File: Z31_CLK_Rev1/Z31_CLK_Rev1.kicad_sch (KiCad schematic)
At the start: 16 parts, among them J1 Conn_01x06_Male, J2 ICSP, U1 MAX6922, U2 4BT-78Z_6L, U3 ATMEGA328-AURCT-ND, U4 MCP2510, U5 TJR1443, Y1 8MHz, Y2 16MHz

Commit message: add code
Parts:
- removed C4: 100n, Capacitor_SMD:C_0805_2012Metric_Pad1.18x1.45mm_HandSolder, symbol Device:C_Small
- removed U1: MAX6922, Package_LCC:PLCC-44_16.6x16.6mm_P1.27mm, symbol Personal:MAX6922
- removed U2: 4BT-78Z_6L, Personal:4BT-78Z_6L, symbol Personal:4BT-78Z_6L

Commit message: Catchup
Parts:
- removed C2, C3: 100n, Capacitor_SMD:C_0805_2012Metric_Pad1.18x1.45mm_HandSolder, symbol Device:C_Small
- removed U4: MCP2510, Package_SO:TSSOP-20_4.4x6.5mm_P0.65mm, symbol Personal:MCP2510
- removed U5: TJR1443, Package_SO:SO-14_3.9x8.65mm_P1.27mm, symbol Personal:TJR1443
- removed Y1: 8MHz, Crystal:Crystal_SMD_HC49-SD, symbol Device:Crystal_Small
- added C1, C2: 100nF, Capacitor_SMD:C_0805_2012Metric_Pad1.18x1.45mm_HandSolder, symbol Device:C
- added C10, C8: 100nF, Capacitor_SMD:C_0805_2012Metric_Pad1.18x1.45mm_HandSolder, symbol Device:C_Small
- added C11: 22uF, Capacitor_SMD:CP_Elec_5x5.7, symbol Device:C_Polarized_Small
- added C12: N/A, Capacitor_SMD:C_0805_2012Metric_Pad1.18x1.45mm_HandSolder, symbol Device:C_Small
- added C13: yes, Capacitor_SMD:C_1210_3225Metric_Pad1.33x2.70mm_HandSolder, symbol Device:C_Small
- added C4: 10pF, Capacitor_SMD:C_0805_2012Metric_Pad1.18x1.45mm_HandSolder, symbol Device:C_Small
- added C9: 1u, Capacitor_SMD:C_1210_3225Metric_Pad1.33x2.70mm_HandSolder, symbol Device:C_Small
- added D1: D_Schottky, Diode_SMD:D_SMA, symbol Device:D_Schottky
- added D2: SMAJ18CAQ-13-F, Diode_SMD:D_SMA, symbol Device:D_TVS
- added F1: Polyfuse, Fuse:Fuse_1812_4532Metric_Pad1.30x3.40mm_HandSolder, symbol Device:Polyfuse
- added R1: 47K, Resistor_SMD:R_0805_2012Metric_Pad1.20x1.40mm_HandSolder, symbol Device:R
- added R2, R3: R, Resistor_SMD:R_0805_2012Metric_Pad1.20x1.40mm_HandSolder, symbol Device:R
- added R4: 10k, Resistor_SMD:R_0805_2012Metric_Pad1.20x1.40mm_HandSolder, symbol Device:R_Small
- added R5, R6: N/A, Resistor_SMD:R_0805_2012Metric_Pad1.20x1.40mm_HandSolder, symbol Device:R_Small
- added SW?: Hour, symbol Switch:SW_Push
- added SW?: Select, symbol Switch:SW_Push
- added SW?: Reset, symbol Switch:SW_Push
- added SW?: Minute, symbol Switch:SW_Push
- added TH1: NTC 47K, Resistor_SMD:R_0805_2012Metric_Pad1.20x1.40mm_HandSolder, symbol Device:Thermistor_NTC
- added U2: HCMS-291x, symbol Personal:HCMS-291x
- added U3: MCP2515-xST, Package_SO:TSSOP-20_4.4x6.5mm_P0.65mm, symbol Interface_CAN_LIN:MCP2515-xST
- added U4: TJR1443, Package_SO:SO-14_3.9x8.65mm_P1.27mm, symbol Personal:TJR1443
- added U5: NCV4276B, Package_TO_SOT_SMD:TO-263-5_TabPin3, symbol Personal:NCV4276B
- added Y2: 8MHz, Crystal:Crystal_SMD_HC49-SD, symbol Device:Crystal_Small
- C5: value 100n -> 10pF
- C6, C7: value 20p -> 100nF
- renumbered C1 to C3, J2 to J1, J1 to J2, U3 to U1, Y2 to Y1
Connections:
- net +12V_CONST: now also F1.2
- net +5V: now also C6.2, C7.2, C12.1, C13.1, C8.2, R1.1, R5.1, U2.10 (V_{LED}), U2.22 (V_{Logic}), U2.3 (V_{LED}), U3.20 (VDD), U4.3 (Vcc), U4.5 (Vio), U5.5 (OUT)
- net CANH: now also U4.13 (CANH)
- net CANL: now also U4.12 (CANL)
- net CAN_INT: now also U3.13 (~{INT})
- net CS_CAN: now also U3.18 (~{CS})
- net GND: now also C5.1, C1.2, C10.2, C11.2, C13.2, C2.2, C4.1, C8.1, C9.2, D2.1 (A1), R3.2, R4.2, R6.2, TH1.2, U2.20 (GND_{Logic}), U2.7 (GND_{LED}), U3.10 (VSS), U4.2 (GND), U5.3 (GND); no longer C5.2
- net MISO: now also U3.17 (SO)
- net MOSI: now also U3.16 (SI)
- net SCK: now also U3.14 (SCK)
- net at U1.20 (AREF): no longer C5.1
- net MODULE_TEMPERATURE: now reaches U1.19 (ADC6)
- net MODULE_TEMPERATURE: now also C1.1, R1.2, TH1.1
- net MODULE_VOLTAGE: now reaches U1.22 (ADC7)
- net MODULE_VOLTAGE: now also C2.1, R2.2, R3.1, U4.9 (WAKE)
- net VFBLANK: no longer names the net of U1.9 (PD5)
- new net: R4.1, U4.7 (INH), U5.2 (~{INH})
- new net: C12.2, R5.2, R6.1, U5.4 (VA)
- new net: SW?.1, SW?.1
- new net: SW?.1, SW?.2 (x2)
- new net: SW?.2, SW?.2
- new net: D1.2 (A), D2.2 (A2), F1.1
- new net: C5.2, U3.9 (OSC1), Y2.1
- new net: C4.2, U3.8 (OSC2), Y2.2
- new net +12V: C10.1, C11.1, C9.1, D1.1 (K), U4.10 (Vbat), U5.1 (IN)
- new net +12V_IGN: R2.1
- new net CAN_EN: U3.12 (~{RX0BF}), U4.6 (EN)
- new net CAN_ERR: U3.4 (~{TX0RTS}), U4.8 (~{ERR})
- new net CAN_STB: U3.11 (~{RX1BF}), U4.14 (~{STB_N})
- new net RESET_CAN: U3.19 (~{RESET})
- new net RXCAN: U3.2 (RXCAN), U4.4 (RXCAN)
- new net TXCAN: U3.1 (TXCAN), U4.1 (TXCAN)
- no-connect marks 0 -> 5
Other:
- moved on the sheet: C3, J2, U1, Y1

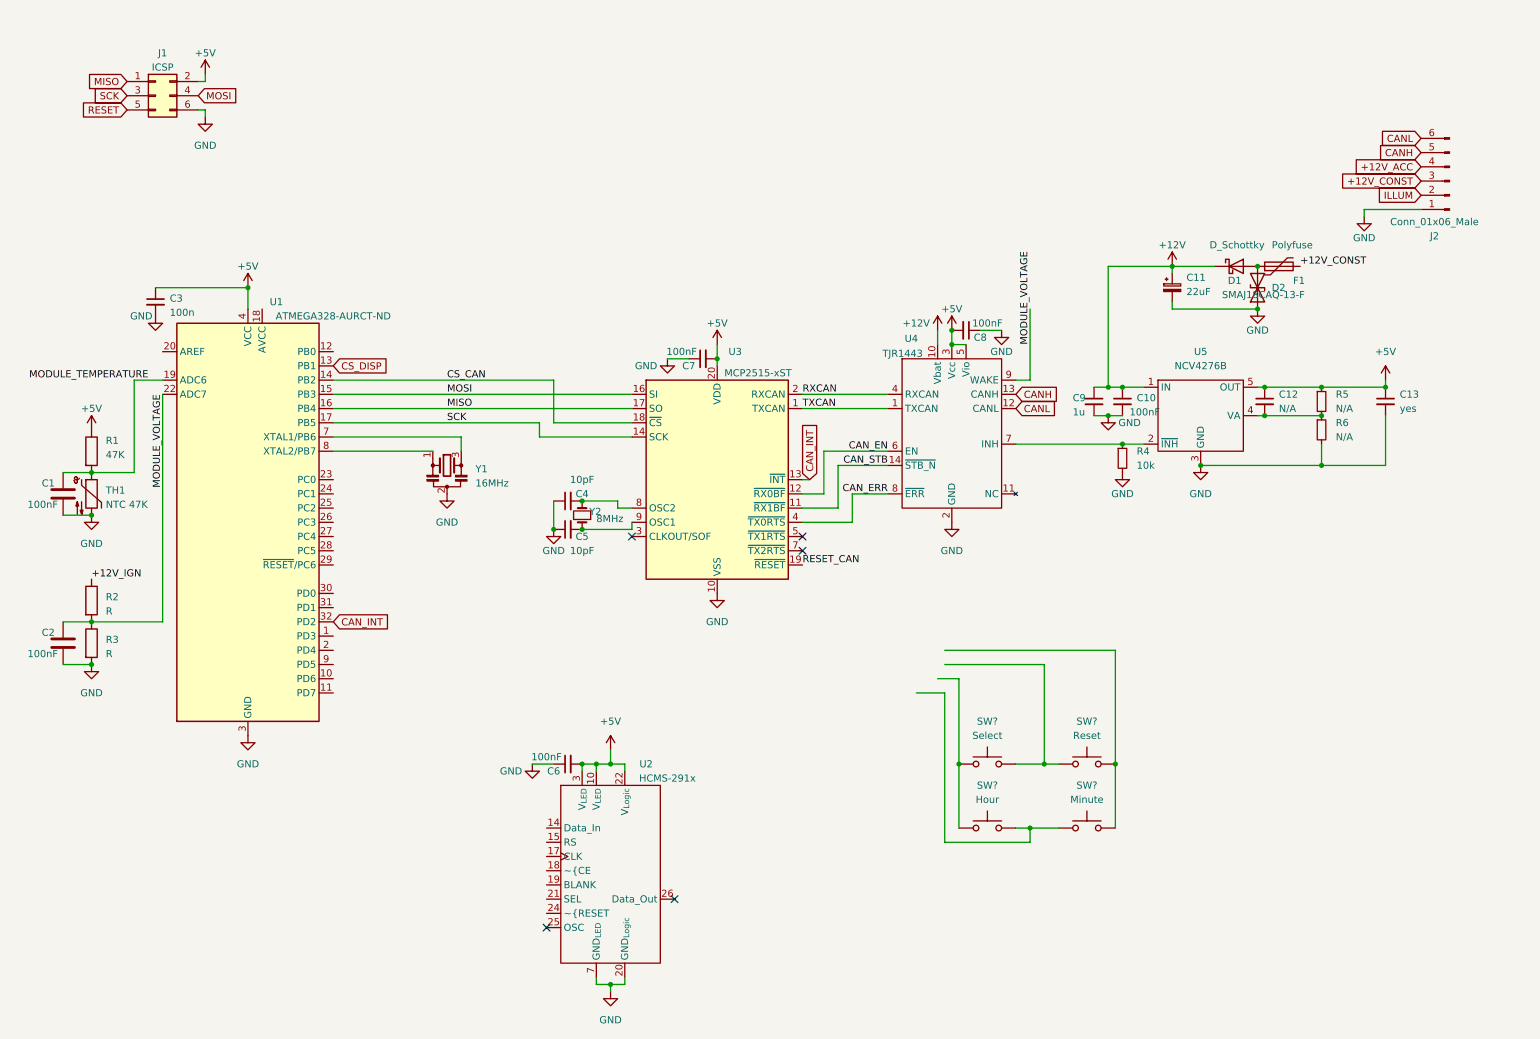
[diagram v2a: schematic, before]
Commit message: Feature-complete Z31-CLK-Rev1; some PCB layout cleanup may still be useful.
Review pending.
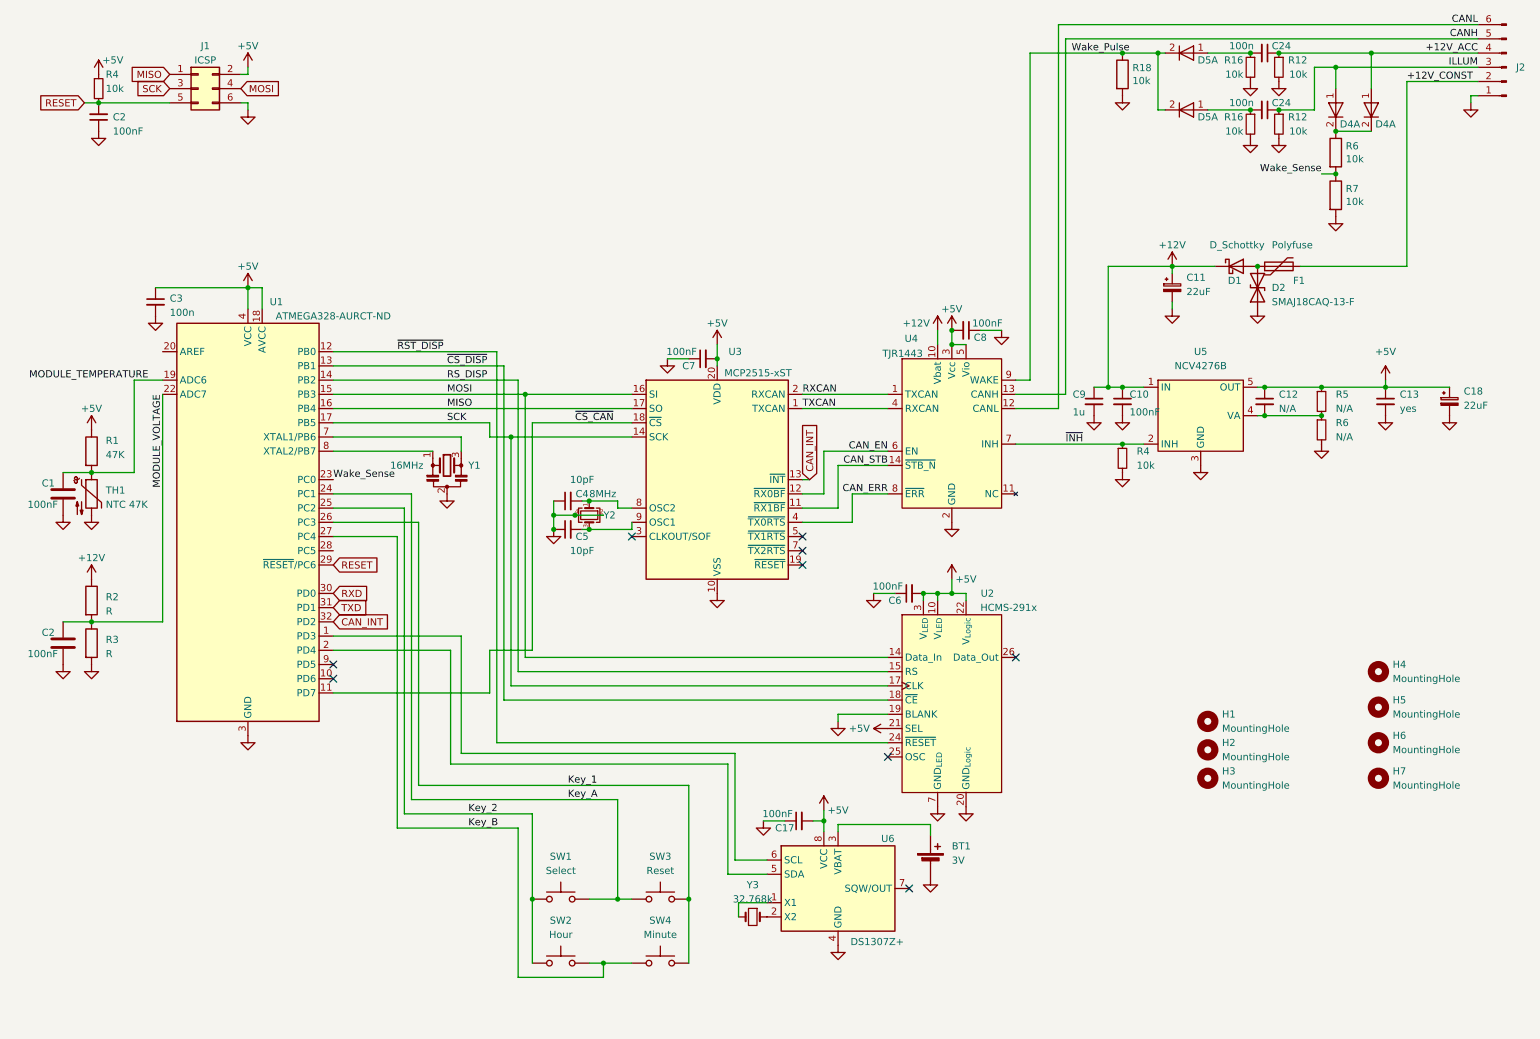
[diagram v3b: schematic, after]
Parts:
- removed Y2: 8MHz, Crystal:Crystal_SMD_HC49-SD, symbol Device:Crystal_Small
- added BT1: 3V, Battery:BatteryHolder_Keystone_500, symbol Device:Battery_Cell
- added C17, C2: 100nF, Capacitor_SMD:C_0805_2012Metric_Pad1.18x1.45mm_HandSolder, symbol Device:C_Small
- added C18: 22uF, Capacitor_SMD:CP_Elec_5x5.7, symbol Device:C_Polarized_Small
- added C24 (x2): 100n, Capacitor_SMD:C_0805_2012Metric_Pad1.18x1.45mm_HandSolder, symbol Device:C_Small
- added D4 (x2), D5 (x2): MMBD4448HCQW, Package_TO_SOT_SMD:SOT-353_SC-70-5, symbol Diode:MMBD4448HCQW
- added H1, H2, H3: MountingHole, MountingHole:MountingHole_2.1mm, symbol Mechanical:MountingHole
- added H4, H5, H6, H7: MountingHole, MountingHole:MountingHole_2.2mm_M2_DIN965, symbol Mechanical:MountingHole
- added R12 (x2), R16 (x2), R4: 10k, Resistor_SMD:R_0805_2012Metric_Pad1.20x1.40mm_HandSolder, symbol Device:R_Small
- added R18, R6, R7: 10k, Resistor_SMD:R_0805_2012Metric_Pad1.20x1.40mm_HandSolder, symbol Device:R
- added U6: DS1307Z+, Package_SO:SOIC-8_3.9x4.9mm_P1.27mm, symbol Timer_RTC:DS1307Z+
- added Y2: 8MHz, Crystal:Crystal_SMD_5032-4Pin_5.0x3.2mm, symbol Device:Crystal_GND24_Small
- added Y3: 32.768k, Crystal:Crystal_AT310_D3.0mm_L10.0mm_Horizontal, symbol Device:Crystal_Small
- SW1, SW2, SW3, SW4: renamed from SW?; footprint (none) -> Personal:membrane_button
- U2: footprint (none) -> Personal:HCMS-291x
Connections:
- net +12V_IGN is gone; now on net +12V: R2.1
- net CS_DISP is gone; now on net ~{CS_DISP}: U1.13 (PB1)
- net +12V_ACC: now also C24.1, D4.1 (A), R12.1
- net +12V_CONST: now also J2.2 (Pin_2); no longer J2.3 (Pin_3)
- net +5V: now also U1.18 (AVCC), U2.21 (SEL), C17.2, C18.1, R4.1, U6.8 (VCC)
- net GND: now also U2.19 (BLANK), BT1.2 (-), C17.1, C18.2, C2.1, R12.2, R12.2, R16.2, R16.2, R18.2, R7.2, U6.4 (GND), Y2.2, Y2.4
- net ILLUM: now also J2.3 (Pin_3), C24.1, D4.1 (A), R12.1; no longer J2.2 (Pin_2)
- net MODULE_VOLTAGE: no longer U4.9 (WAKE)
- net MOSI: now also U2.14 (Data_In)
- net RESET: now also U1.29 (~{RESET}/PC6), C2.2, R4.2
- net RXCAN: now also U4.1 (TXCAN); no longer U4.4 (RXCAN)
- net SCK: now also U2.17 (CLK)
- net TXCAN: now also U4.4 (RXCAN); no longer U4.1 (TXCAN)
- net ~{INH}: now reaches R4.1, U4.7 (INH), U5.2 (INH)
- net Key_2: now reaches SW1.1, SW2.1
- net Key_2: now also U1.25 (PC2)
- net Key_B: now reaches SW2.2, SW4.1
- net Key_B: now also U1.27 (PC4)
- net Key_A: now reaches SW1.2, SW3.1
- net Key_A: now also U1.24 (PC1)
- net Key_1: now reaches SW3.2, SW4.2
- net Key_1: now also U1.26 (PC3)
- net at C5.2, U3.9 (OSC1): now also Y2.3
- net at C4.2, U3.8 (OSC2): now also Y2.1
- net at U1.1 (PD3): now also U6.6 (SCL)
- net ~{CS_CAN}: now reaches U1.11 (PD7)
- net ~{CS_CAN}: now also U3.18 (~{CS})
- net ~{RST_DISP}: now reaches U1.12 (PB0)
- net ~{RST_DISP}: now also U2.24 (~{RESET})
- net at U1.2 (PD4): now also U6.5 (SDA)
- net Wake_Sense: now reaches U1.23 (PC0)
- net Wake_Sense: now also R6.2, R7.1
- net RXD: now reaches U1.30 (PD0)
- net TXD: now reaches U1.31 (PD1)
- net RS_DISP: now reaches U2.15 (RS)
- net RS_DISP: now also U1.14 (PB2)
- net ~{CS_DISP}: now reaches U2.18 (~{CE})
- removed net CS_CAN: U1.14 (PB2), U3.18 (~{CS})
- net RESET_CAN: no longer names the net of U3.19 (~{RESET})
- new net: C24.2, D5.1 (A), R16.1 (x2)
- new net: U6.2 (X2), Y3.1
- new net: U6.1 (X1), Y3.2
- new net: D4.2 (K), D4.2 (K), R6.1
- new net: BT1.1 (+), U6.3 (VBAT)
- new net Wake_Pulse: D5.2 (K), D5.2 (K), R18.1, U4.9 (WAKE)
- no-connect marks 5 -> 9
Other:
- moved on the sheet: C6, J1, J2, SW1, SW2, SW3, SW4
